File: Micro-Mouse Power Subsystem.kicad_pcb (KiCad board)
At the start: 2 copper layers, 12 parts, among them J1 Pin Header, J2 TYPE-C-31-M-12

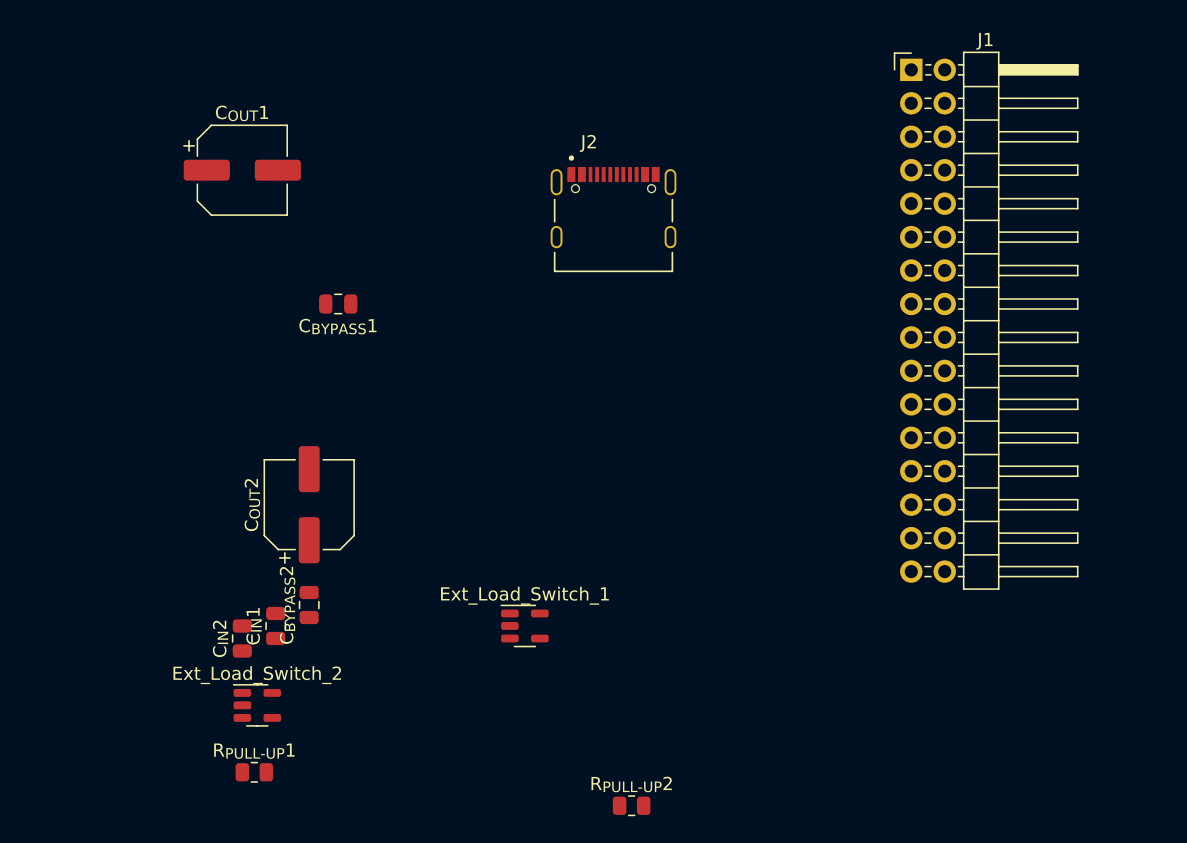
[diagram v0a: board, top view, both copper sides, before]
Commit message: V1
- 2x ext load switching is now implemented using mosfets

- 4 bidirectional motors done

- Assigned JLCP components

- Just moved components into groups in PCB mode to make it easier for when we have to add wires
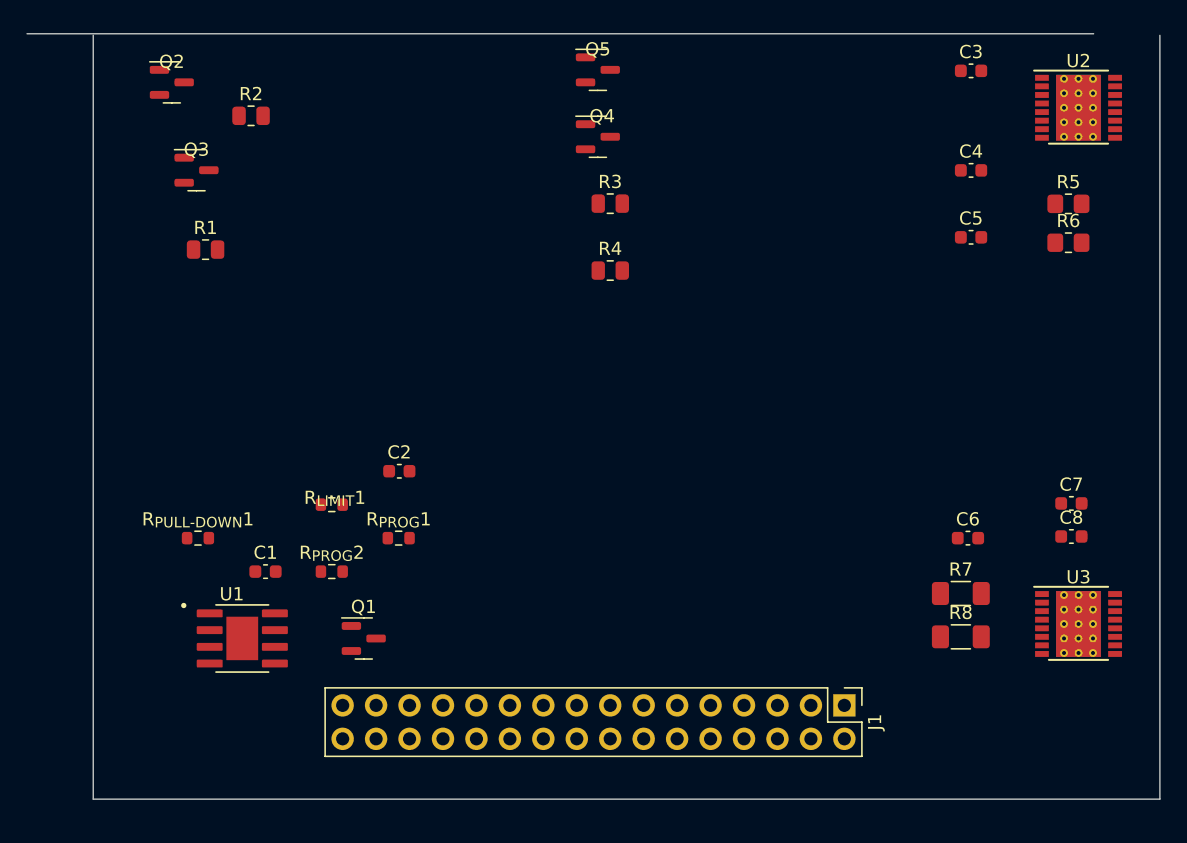
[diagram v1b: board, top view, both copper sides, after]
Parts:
- removed C_{BYPASS}1, C_{BYPASS}2: 0.1uF, Capacitor_SMD:C_0805_2012Metric
- removed C_{IN}1, C_{IN}2: 1uF, Capacitor_SMD:C_0805_2012Metric
- removed C_{OUT}1, C_{OUT}2: 120uF, Capacitor_SMD:CP_Elec_6.3x7.7
- removed Ext_Load_Switch_1, Ext_Load_Switch_2: AP22814AW5-7, Package_TO_SOT_SMD:SOT-23-5
- removed J2: TYPE-C-31-M-12, TYPE-C-31-M-12:HRO_TYPE-C-31-M-12
- removed R_{PULL-UP}1, R_{PULL-UP}2: 10K, Resistor_SMD:R_0805_2012Metric
- added C1: C_{CHARGE_IN}, Capacitor_SMD:C_0603_1608Metric, F.Cu at (118.6, 109.2)
- added C2: C_Small, Capacitor_SMD:C_0603_1608Metric, F.Cu at (128.8, 101.6)
- added C3: 2.2uF, Capacitor_SMD:C_0603_1608Metric, F.Cu at (172.2, 71.2)
- added C4: 10uF, Capacitor_SMD:C_0603_1608Metric, F.Cu at (172.2, 78.8)
- added C5: 0.01uF, Capacitor_SMD:C_0603_1608Metric, F.Cu at (172.2, 83.8)
- added C6: 0.01uF, Capacitor_SMD:C_0603_1608Metric, F.Cu at (171.9, 106.7)
- added C7: 2.2uF, Capacitor_SMD:C_0603_1608Metric, F.Cu at (179.8, 104.0)
- added C8: 10uF, Capacitor_SMD:C_0603_1608Metric, F.Cu at (179.8, 106.6)
- added Q1: 2N7002, Package_TO_SOT_SMD:SOT-23, F.Cu at (126.1, 114.3)
- added Q2: AO3401A, Package_TO_SOT_SMD:SOT-23, F.Cu at (111.5, 72.1)
- added Q3: AO3400A, Package_TO_SOT_SMD:SOT-23, F.Cu at (113.4, 78.7)
- added Q4: AO3400A, Package_TO_SOT_SMD:SOT-23, F.Cu at (143.8, 76.2)
- added Q5: AO3401A, Package_TO_SOT_SMD:SOT-23, F.Cu at (143.8, 71.1)
- added R1: 1M, Resistor_SMD:R_0805_2012Metric, F.Cu at (114.1, 84.8)
- added R2: 220, Resistor_SMD:R_0805_2012Metric, F.Cu at (117.5, 74.6)
- added R3: 220, Resistor_SMD:R_0805_2012Metric, F.Cu at (144.8, 81.3)
- added R4: 1M, Resistor_SMD:R_0805_2012Metric, F.Cu at (144.8, 86.4)
- added R5: 1, Resistor_SMD:R_0805_2012Metric_Pad1.20x1.40mm_HandSolder, F.Cu at (179.6, 81.3)
- added R6: 1, Resistor_SMD:R_0805_2012Metric_Pad1.20x1.40mm_HandSolder, F.Cu at (179.6, 84.2)
- added R7: 0.4, Resistor_SMD:R_1206_3216Metric_Pad1.30x1.75mm_HandSolder, F.Cu at (171.4, 110.9)
- added R8: 0.4, Resistor_SMD:R_1206_3216Metric_Pad1.30x1.75mm_HandSolder, F.Cu at (171.4, 114.2)
- added R_{LIMIT}1: 1k, Resistor_SMD:R_0603_1608Metric, F.Cu at (123.6, 104.1)
- added R_{PROG}1: 6k, Resistor_SMD:R_0603_1608Metric, F.Cu at (128.7, 106.7)
- added R_{PROG}2: 3k, Resistor_SMD:R_0603_1608Metric, F.Cu at (123.6, 109.2)
- added R_{PULL-DOWN}1: 10k, Resistor_SMD:R_0603_1608Metric, F.Cu at (113.5, 106.7)
- added U1: TP4056, TP4056:SOP127P600X175-9N, F.Cu at (116.8, 114.3)
- added U2: brushed DC motors, Package_SO:HTSSOP-16-1EP_4.4x5mm_P0.65mm_EP3.4x5mm_Mask3x3mm_ThermalVias, F.Cu at (180.3, 74.0)
- added U3: auxiliary motors, Package_SO:HTSSOP-16-1EP_4.4x5mm_P0.65mm_EP3.4x5mm_Mask3x3mm_ThermalVias, F.Cu at (180.3, 113.2)
- J1: footprint Connector_PinHeader_2.54mm:PinHeader_2x16_P2.54mm_Horizontal -> Connector_PinHeader_2.54mm:PinHeader_2x16_P2.54mm_Vertical
- moved J1 48.5 mm to (162.6, 119.4), turned to -90 degrees
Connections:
- net /Motor2_B_OUT  renamed /Motor2_B_OUT
- net /Motor4_B_OUT  renamed /Motor4_B_OUT
- J1 pad 10: /MOTOR4_CTRL2  -> /MOTOR4_CTRL2
- J1 pad 24: /MOTOR3_CTRL1  -> /MOTOR3_CTRL1
- J1 pad 26: /MOTOR3_CTRL2  -> /MOTOR3_CTRL2
- J1 pad 27: /MOTOR3_A_OUT  -> /MOTOR3_A_OUT
- J1 pad 28: /MOTOR1_CTRL1  -> /MOTOR1_CTRL1
- J1 pad 29: /MOTOR3_B_OUT  -> /MOTOR3_B_OUT
- J1 pad 30: /MOTOR1_CTRL2  -> /MOTOR1_CTRL2
- J1 pad 31: /MOTOR1_B_OUT  -> /MOTOR1_B_OUT
- J1 pad 4: /MOTOR2_CTRL1  -> /MOTOR2_CTRL1
- J1 pad 6: /MOTOR2_CTRL2  -> /MOTOR2_CTRL2
- J1 pad 8: /MOTOR4_CTRL1  -> /MOTOR4_CTRL1
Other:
- board outline added: 86 x 58.1 mm

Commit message: V1.1
- Refined Motor drivers
- Added USBC
- Added JST (don't know connections yet)
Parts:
- removed C1: C_{CHARGE_IN}, Capacitor_SMD:C_0603_1608Metric
- removed C2: C_Small, Capacitor_SMD:C_0603_1608Metric
- removed C3, C7: 2.2uF, Capacitor_SMD:C_0603_1608Metric
- removed C4, C8: 10uF, Capacitor_SMD:C_0603_1608Metric
- removed C5, C6: 0.01uF, Capacitor_SMD:C_0603_1608Metric
- removed J1: Pin Header, Connector_PinHeader_2.54mm:PinHeader_2x16_P2.54mm_Vertical
- removed Q1: 2N7002, Package_TO_SOT_SMD:SOT-23
- removed Q2, Q5: AO3401A, Package_TO_SOT_SMD:SOT-23
- removed Q3, Q4: AO3400A, Package_TO_SOT_SMD:SOT-23
- removed R1, R4: 1M, Resistor_SMD:R_0805_2012Metric
- removed R2, R3: 220, Resistor_SMD:R_0805_2012Metric
- removed R5, R6: 1, Resistor_SMD:R_0805_2012Metric_Pad1.20x1.40mm_HandSolder
- removed R7, R8: 0.4, Resistor_SMD:R_1206_3216Metric_Pad1.30x1.75mm_HandSolder
- removed R_{LIMIT}1: 1k, Resistor_SMD:R_0603_1608Metric
- removed R_{PROG}1: 6k, Resistor_SMD:R_0603_1608Metric
- removed R_{PROG}2: 3k, Resistor_SMD:R_0603_1608Metric
- removed R_{PULL-DOWN}1: 10k, Resistor_SMD:R_0603_1608Metric
- removed U1: TP4056, TP4056:SOP127P600X175-9N
- removed U2: brushed DC motors, Package_SO:HTSSOP-16-1EP_4.4x5mm_P0.65mm_EP3.4x5mm_Mask3x3mm_ThermalVias
- removed U3: auxiliary motors, Package_SO:HTSSOP-16-1EP_4.4x5mm_P0.65mm_EP3.4x5mm_Mask3x3mm_ThermalVias
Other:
- board outline removed

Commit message: Update to KiCad 9.0
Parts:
- added C1: C_{CHARGE_IN}, Capacitor_SMD:C_0603_1608Metric, F.Cu at (145.4, 108.2)
- added C2: C_Small, Capacitor_SMD:C_0603_1608Metric, F.Cu at (145.4, 110.8)
- added C3: 2.2uF, Capacitor_SMD:C_0603_1608Metric, F.Cu at (145.4, 113.3)
- added C4: 10uF, Capacitor_SMD:C_0603_1608Metric, F.Cu at (145.4, 115.8)
- added C5: 0.01uF, Capacitor_SMD:C_0603_1608Metric, F.Cu at (145.4, 118.3)
- added C6: 0.01uF, Capacitor_SMD:C_0603_1608Metric, F.Cu at (149.4, 108.2)
- added C7: 2.2uF, Capacitor_SMD:C_0603_1608Metric, F.Cu at (149.4, 110.8)
- added C8: 10uF, Capacitor_SMD:C_0603_1608Metric, F.Cu at (149.4, 113.3)
- added C9: 1uF, Capacitor_SMD:C_0603_1608Metric, F.Cu at (149.4, 115.8)
- added J1: Pin Header, Connector_PinHeader_2.54mm:PinHeader_2x16_P2.54mm_Vertical, F.Cu at (133.6, 91.4)
- added J2: TYPE-C-31-M-12, Connector_USB:USB_C_Receptacle_HRO_TYPE-C-31-M-12, F.Cu at (149.2, 125.3)
- added J3: Conn_01x02, Connector_JST:JST_PH_S2B-PH-K_1x02_P2.00mm_Horizontal, F.Cu at (158.0, 121.9)
- added Q1: 2N7002, Package_TO_SOT_SMD:SOT-23, F.Cu at (140.9, 91.5)
- added Q2: AO3401A, Package_TO_SOT_SMD:SOT-23, F.Cu at (140.9, 96.1)
- added Q3: AO3400A, Package_TO_SOT_SMD:SOT-23, F.Cu at (140.9, 100.8)
- added Q4: AO3400A, Package_TO_SOT_SMD:SOT-23, F.Cu at (140.9, 105.4)
- added Q5: AO3401A, Package_TO_SOT_SMD:SOT-23, F.Cu at (140.9, 110.0)
- added R1: 1M, Resistor_SMD:R_0805_2012Metric, F.Cu at (157.6, 108.5)
- added R2: 220, Resistor_SMD:R_0805_2012Metric, F.Cu at (157.6, 111.4)
- added R3: 220, Resistor_SMD:R_0805_2012Metric, F.Cu at (157.6, 114.4)
- added R4: 1M, Resistor_SMD:R_0805_2012Metric, F.Cu at (157.6, 117.3)
- added R5: 1, Resistor_SMD:R_0805_2012Metric_Pad1.20x1.40mm_HandSolder, F.Cu at (160.9, 101.8)
- added R6: 1, Resistor_SMD:R_0805_2012Metric_Pad1.20x1.40mm_HandSolder, F.Cu at (160.9, 104.8)
- added R7: 0.4, Resistor_SMD:R_1206_3216Metric_Pad1.30x1.75mm_HandSolder, F.Cu at (155.6, 102.0)
- added R8: 0.4, Resistor_SMD:R_1206_3216Metric_Pad1.30x1.75mm_HandSolder, F.Cu at (155.6, 105.3)
- added R9: 75K, Resistor_SMD:R_0603_1608Metric, F.Cu at (149.4, 118.3)
- added R_{LIMIT}1: 1k, Resistor_SMD:R_0603_1608Metric, F.Cu at (153.4, 108.2)
- added R_{PROG}1: 6k, Resistor_SMD:R_0603_1608Metric, F.Cu at (153.4, 110.8)
- added R_{PROG}2: 3k, Resistor_SMD:R_0603_1608Metric, F.Cu at (153.4, 113.3)
- added R_{PULL-DOWN}1: 10k, Resistor_SMD:R_0603_1608Metric, F.Cu at (153.4, 115.8)
- added SW1: SW_SPDT, Connector_Wire:SolderWire-0.75sqmm_1x03_P4.8mm_D1.25mm_OD2.3mm, F.Cu at (145.8, 91.4)
- added TP1: VG1, TestPoint:TestPoint_Pad_1.5x1.5mm, F.Cu at (140.2, 114.0)
- added TP2: VG2, TestPoint:TestPoint_Pad_1.5x1.5mm, F.Cu at (140.2, 117.5)
- added TP3: Fault1, TestPoint:TestPoint_Pad_1.5x1.5mm, F.Cu at (140.2, 121.1)
- added TP4: Fault2, TestPoint:TestPoint_Pad_1.5x1.5mm, F.Cu at (140.2, 124.7)
- added TP5: HV (9V), TestPoint:TestPoint_Pad_1.5x1.5mm, F.Cu at (140.2, 128.2)
- added U1: TP4056, TP4056:SOP127P600X175-9N, F.Cu at (157.7, 97.0)
- added U2: brushed DC motors, Package_SO:HTSSOP-16-1EP_4.4x5mm_P0.65mm_EP3.4x5mm_Mask2.46x2.31mm_ThermalVias, F.Cu at (148.2, 97.0)
- added U3: auxiliary motors, Package_SO:HTSSOP-16-1EP_4.4x5mm_P0.65mm_EP3.4x5mm_Mask2.46x2.31mm_ThermalVias, F.Cu at (148.2, 103.7)
- added U4: HUSB237-AA001-DN06R, Package_DFN_QFN:DFN-6-1EP_2x2mm_P0.65mm_EP1x1.6mm, F.Cu at (160.2, 91.0)

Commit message: V2
- all schematics are uploaded
- missing a few footprints from Sinaye
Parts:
- removed C1: C_{CHARGE_IN}, Capacitor_SMD:C_0603_1608Metric
- removed C2: C_Small, Capacitor_SMD:C_0603_1608Metric
- removed C3, C7: 2.2uF, Capacitor_SMD:C_0603_1608Metric
- removed C4, C8: 10uF, Capacitor_SMD:C_0603_1608Metric
- removed C5, C6: 0.01uF, Capacitor_SMD:C_0603_1608Metric
- removed C9: 1uF, Capacitor_SMD:C_0603_1608Metric
- removed J1: Pin Header, Connector_PinHeader_2.54mm:PinHeader_2x16_P2.54mm_Vertical
- removed J2: TYPE-C-31-M-12, Connector_USB:USB_C_Receptacle_HRO_TYPE-C-31-M-12
- removed J3: Conn_01x02, Connector_JST:JST_PH_S2B-PH-K_1x02_P2.00mm_Horizontal
- removed Q1: 2N7002, Package_TO_SOT_SMD:SOT-23
- removed Q2, Q5: AO3401A, Package_TO_SOT_SMD:SOT-23
- removed Q3, Q4: AO3400A, Package_TO_SOT_SMD:SOT-23
- removed R1, R4: 1M, Resistor_SMD:R_0805_2012Metric
- removed R2, R3: 220, Resistor_SMD:R_0805_2012Metric
- removed R5, R6: 1, Resistor_SMD:R_0805_2012Metric_Pad1.20x1.40mm_HandSolder
- removed R7, R8: 0.4, Resistor_SMD:R_1206_3216Metric_Pad1.30x1.75mm_HandSolder
- removed R9: 75K, Resistor_SMD:R_0603_1608Metric
- removed R_{LIMIT}1: 1k, Resistor_SMD:R_0603_1608Metric
- removed R_{PROG}1: 6k, Resistor_SMD:R_0603_1608Metric
- removed R_{PROG}2: 3k, Resistor_SMD:R_0603_1608Metric
- removed R_{PULL-DOWN}1: 10k, Resistor_SMD:R_0603_1608Metric
- removed SW1: SW_SPDT, Connector_Wire:SolderWire-0.75sqmm_1x03_P4.8mm_D1.25mm_OD2.3mm
- removed TP1: VG1, TestPoint:TestPoint_Pad_1.5x1.5mm
- removed TP2: VG2, TestPoint:TestPoint_Pad_1.5x1.5mm
- removed TP3: Fault1, TestPoint:TestPoint_Pad_1.5x1.5mm
- removed TP4: Fault2, TestPoint:TestPoint_Pad_1.5x1.5mm
- removed TP5: HV (9V), TestPoint:TestPoint_Pad_1.5x1.5mm
- removed U1: TP4056, TP4056:SOP127P600X175-9N
- removed U2: brushed DC motors, Package_SO:HTSSOP-16-1EP_4.4x5mm_P0.65mm_EP3.4x5mm_Mask2.46x2.31mm_ThermalVias
- removed U3: auxiliary motors, Package_SO:HTSSOP-16-1EP_4.4x5mm_P0.65mm_EP3.4x5mm_Mask2.46x2.31mm_ThermalVias
- removed U4: HUSB237-AA001-DN06R, Package_DFN_QFN:DFN-6-1EP_2x2mm_P0.65mm_EP1x1.6mm

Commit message: Added footprints and adjusted labelling
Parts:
- added C10: 1uF, Capacitor_SMD:C_0805_2012Metric, F.Cu at (118.8, 63.1)
- added C3: 2.2uF, Capacitor_SMD:C_0603_1608Metric, F.Cu at (140.7, 62.8)
- added C4: 10uF, Capacitor_SMD:C_0603_1608Metric, F.Cu at (140.7, 65.3)
- added C5: 0.01uF, Capacitor_SMD:C_0603_1608Metric, F.Cu at (140.7, 67.8)
- added C6: 0.01uF, Capacitor_SMD:C_0603_1608Metric, F.Cu at (140.7, 70.4)
- added C7: 2.2uF, Capacitor_SMD:C_0603_1608Metric, F.Cu at (140.7, 72.9)
- added C8: 10uF, Capacitor_SMD:C_0603_1608Metric, F.Cu at (140.7, 75.4)
- added C9: 1uF, Capacitor_SMD:C_0603_1608Metric, F.Cu at (140.7, 77.9)
- added C_{1}1: 1uF, Capacitor_SMD:C_0805_2012Metric, F.Cu at (118.8, 66.1)
- added C_{BOOT}1: 0.1uF, Capacitor_SMD:C_0805_2012Metric, F.Cu at (118.8, 69.1)
- added C_{BYPASS}1: 0.1u, Capacitor_SMD:C_0805_2012Metric, F.Cu at (118.8, 72.1)
- added C_{BY}1: 0.1uF, Capacitor_SMD:C_0805_2012Metric, F.Cu at (118.8, 75.1)
- added C_{CHARGE_IN}1: 10u, Capacitor_SMD:C_0603_1608Metric, F.Cu at (144.7, 62.8)
- added C_{CHARGE_OUT}1: 10u, Capacitor_SMD:C_0603_1608Metric, F.Cu at (144.7, 65.3)
- added C_{COMP}1: 1nF, Capacitor_SMD:C_0805_2012Metric, F.Cu at (118.8, 78.1)
- added C_{IN_3.3}1: 100uF, Capacitor_SMD:C_1206_3216Metric, F.Cu at (123.9, 63.2)
- added C_{IN_3.3}2: 100uF, Capacitor_SMD:C_1206_3216Metric, F.Cu at (123.9, 66.6)
- added C_{IN_3.3}3: 22uF, Capacitor_SMD:C_0603_1608Metric, F.Cu at (144.7, 67.8)
- added C_{IN_5}1: 10uF, Capacitor_SMD:C_0805_2012Metric, F.Cu at (118.8, 81.1)
- added C_{IN}1: 100uF, Capacitor_SMD:C_1210_3225Metric, F.Cu at (153.6, 63.7)
- added C_{IN}2: 100uF, Capacitor_SMD:C_1210_3225Metric, F.Cu at (153.6, 68.0)
- added C_{IN}3: 22uF, Capacitor_SMD:C_1206_3216Metric, F.Cu at (123.9, 70.0)
- added C_{OUT_3.3}1: 100uF, Capacitor_SMD:C_1206_3216Metric, F.Cu at (123.9, 73.3)
- added C_{OUT_3.3}2: 100uF, Capacitor_SMD:C_1206_3216Metric, F.Cu at (123.9, 76.7)
- added C_{OUT_3.3}3: 100uF, Capacitor_SMD:C_1206_3216Metric, F.Cu at (123.9, 80.0)
- added C_{OUT}1: 100uF, Capacitor_SMD:C_1210_3225Metric, F.Cu at (153.6, 72.2)
- added C_{OUT}2: 100uF, Capacitor_SMD:C_1210_3225Metric, F.Cu at (153.6, 76.5)
- added C_{OUT}3: 100uF, Capacitor_SMD:C_1206_3216Metric, F.Cu at (123.9, 83.3)
- added C_{OUT}4: 22uF, Capacitor_SMD:C_0603_1608Metric, F.Cu at (144.7, 70.4)
- added C_{OUT}5: 22uF, Capacitor_SMD:C_0603_1608Metric, F.Cu at (144.7, 72.9)
- added C_{OUT}6: 22uF, Capacitor_SMD:C_0603_1608Metric, F.Cu at (144.7, 75.4)
- added C_{SS}1: 47nF, Capacitor_SMD:C_0805_2012Metric, F.Cu at (118.8, 84.2)
- added J1: Pin Header, Connector_PinHeader_2.54mm:PinHeader_2x16_P2.54mm_Vertical, F.Cu at (111.7, 63.9)
- added J2: TYPE-C-31-M-12, Connector_USB:USB_C_Receptacle_HRO_TYPE-C-31-M-12, F.Cu at (132.5, 101.9)
- added J3: Conn_01x02, Connector_JST:JST_PH_S2B-PH-K_1x02_P2.00mm_Horizontal, F.Cu at (142.9, 101.6)
- added L1: L, Inductor_SMD:L_0805_2012Metric, F.Cu at (151.4, 96.8)
- added Q1: 2N7002, Package_TO_SOT_SMD:SOT-23, F.Cu at (123.5, 87.4)
- added Q2: AO3401A, Package_TO_SOT_SMD:SOT-23, F.Cu at (123.5, 92.0)
- added Q3: AO3400A, Package_TO_SOT_SMD:SOT-23, F.Cu at (123.5, 96.7)
- added Q4: AO3400A, Package_TO_SOT_SMD:SOT-23, F.Cu at (123.5, 101.3)
- added Q5: AO3401A, Package_TO_SOT_SMD:SOT-23, F.Cu at (123.5, 105.9)
- added R1: 1M, Resistor_SMD:R_0805_2012Metric, F.Cu at (128.9, 82.8)
- added R2: 220, Resistor_SMD:R_0805_2012Metric, F.Cu at (128.9, 85.7)
- added R3: 220, Resistor_SMD:R_0805_2012Metric, F.Cu at (128.9, 88.7)
- added R4: 1M, Resistor_SMD:R_0805_2012Metric, F.Cu at (128.9, 91.6)
- added R5: 1, Resistor_SMD:R_0805_2012Metric_Pad1.20x1.40mm_HandSolder, F.Cu at (151.5, 87.4)
- added R6: 1, Resistor_SMD:R_0805_2012Metric_Pad1.20x1.40mm_HandSolder, F.Cu at (151.5, 90.3)
- added R7: 0.4, Resistor_SMD:R_1206_3216Metric_Pad1.30x1.75mm_HandSolder, F.Cu at (150.8, 100.8)
- added R8: 0.4, Resistor_SMD:R_1206_3216Metric_Pad1.30x1.75mm_HandSolder, F.Cu at (150.8, 104.1)
- added R9: 75K, Resistor_SMD:R_0603_1608Metric, F.Cu at (144.7, 77.9)
- added R_{COMP}1: 68k, Resistor_SMD:R_0805_2012Metric, F.Cu at (128.9, 94.6)
- added R_{FB}1: 150k, Resistor_SMD:R_0805_2012Metric, F.Cu at (133.3, 82.8)
- added R_{FB}2: 47k, Resistor_SMD:R_0805_2012Metric, F.Cu at (133.3, 85.7)
- added R_{FSW}1: 220k, Resistor_SMD:R_0805_2012Metric, F.Cu at (133.3, 88.7)
- added R_{FSW}2: 33k, Resistor_SMD:R_0805_2012Metric, F.Cu at (133.3, 91.6)
- added R_{ILIM}1: 100k, Resistor_SMD:R_0805_2012Metric, F.Cu at (133.3, 94.6)
- added R_{LIMIT}1: 1k, Resistor_SMD:R_0603_1608Metric, F.Cu at (148.7, 62.8)
- added R_{PROG}1: 5.6k, Resistor_SMD:R_0603_1608Metric, F.Cu at (148.7, 65.3)
- added R_{PROG}2: 2.7k, Resistor_SMD:R_0603_1608Metric, F.Cu at (148.7, 67.8)
- added R_{PULL_DOWN}1: 10k, Resistor_SMD:R_0603_1608Metric, F.Cu at (148.7, 70.4)
- added R_{SCL}1: 4.7k, Resistor_SMD:R_0805_2012Metric, F.Cu at (137.7, 82.8)
- added R_{SDA}1: 4.7k, Resistor_SMD:R_0805_2012Metric, F.Cu at (137.7, 85.7)
- added R_{SHUNT}1: 0.075, Resistor_SMD:R_0805_2012Metric, F.Cu at (137.7, 88.7)
- added SW1: SW_SPDT, Connector_Wire:SolderWire-0.75sqmm_1x03_P4.8mm_D1.25mm_OD2.3mm, F.Cu at (142.3, 83.6)
- added TP1: VG1, TestPoint:TestPoint_Pad_1.5x1.5mm, F.Cu at (136.9, 63.4)
- added TP2: VG2, TestPoint:TestPoint_Pad_1.5x1.5mm, F.Cu at (136.9, 66.9)
- added TP3: Fault1, TestPoint:TestPoint_Pad_1.5x1.5mm, F.Cu at (136.9, 70.5)
- added TP4: Fault2, TestPoint:TestPoint_Pad_1.5x1.5mm, F.Cu at (136.9, 74.0)
- added TP5: HV (9V), TestPoint:TestPoint_Pad_1.5x1.5mm, F.Cu at (136.9, 77.5)
- added U1: TP4056-42-ESOP8, Package_SO:SOIC-8-1EP_3.9x4.9mm_P1.27mm_EP2.41x3.3mm_ThermalVias, F.Cu at (130.9, 64.9)
- added U2: brushed DC motors, Package_SO:HTSSOP-16-1EP_4.4x5mm_P0.65mm_EP3.4x5mm_Mask2.46x2.31mm_ThermalVias, F.Cu at (144.7, 89.2)
- added U3: auxiliary motors, Package_SO:HTSSOP-16-1EP_4.4x5mm_P0.65mm_EP3.4x5mm_Mask2.46x2.31mm_ThermalVias, F.Cu at (144.7, 95.9)
- added U4: HUSB237-AA001-DN06R, Package_DFN_QFN:DFN-6-1EP_2x2mm_P0.65mm_EP1x1.6mm, F.Cu at (151.5, 93.7)
- added U7: XL1509-3.3, Package_SO:SOIC-8_3.9x4.9mm_P1.27mm, F.Cu at (130.9, 71.5)
- added U8: XL1509-5.0, Package_SO:SOIC-8_3.9x4.9mm_P1.27mm, F.Cu at (130.9, 78.1)

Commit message: pcb
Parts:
- moved C_{OUT_3.3}2 131.6 mm to (254.1, 57.8), turned to 90 degrees
- moved C_{OUT_3.3}1 128.6 mm to (251.5, 57.8), turned to 90 degrees
- moved C_{OUT_3.3}3 127.1 mm to (249.0, 57.8), turned to 90 degrees
- moved TP4 121.2 mm to (251.9, 35.5)
- moved C10 121.0 mm to (239.8, 62.9), turned to 180 degrees
- moved C_{IN_3.3}2 120.4 mm to (243.9, 57.8)
- moved C_{IN_3.3}1 120.3 mm to (243.9, 55.2)
- moved J2 119.9 mm to (250.0, 77.5), turned to -90 degrees
- moved U3 119.1 mm to (249.7, 39.6), turned to 180 degrees
- moved C9 118.7 mm to (259.4, 78.5), turned to 90 degrees
- moved R7 118.2 mm to (255.4, 45.7)
- moved R8 118.2 mm to (255.4, 48.9)
- moved TP5 117.5 mm to (254.3, 70.9)
- moved Q4 114.9 mm to (237.8, 90.3)
- moved Q5 114.9 mm to (237.8, 94.9), turned to -90 degrees
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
